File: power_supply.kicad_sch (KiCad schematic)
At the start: 59 parts, among them Q1201 2N7002, Q1202 DMP3037LSS, U1201 TL431PK, U1202 TL431PK, U1203 TL431PK, U1204 MCP1825T-330, U1205 NCV8164ASN120T1G, U1206 MCP1825T-330, U1207 NCV8164ASN250T1G, U1208 NCV8164ASN330T1G

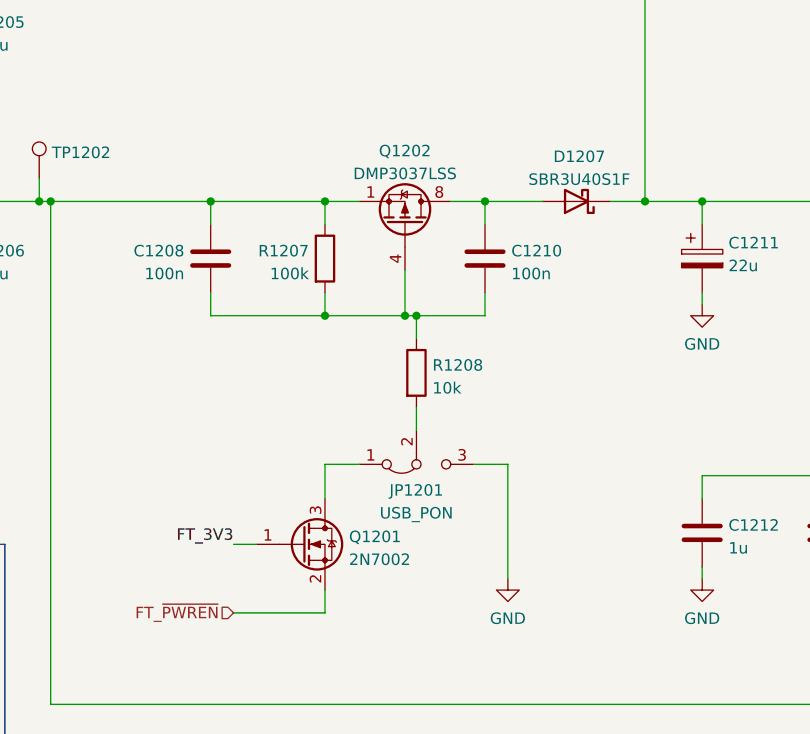
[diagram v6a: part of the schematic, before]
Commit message: Schematic: change mosfets in VBUS switcher
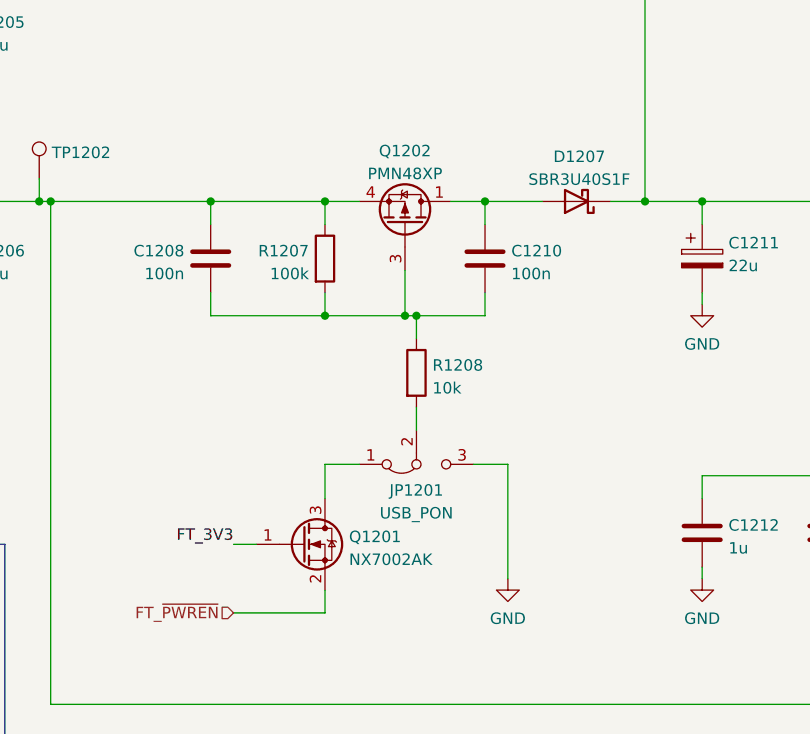
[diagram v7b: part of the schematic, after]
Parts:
- removed Q1202: DMP3037LSS, Package_SO:SOIC-8_3.9x4.9mm_P1.27mm, symbol Transistor_FET:FDS9435A
- added Q1202: PMN48XP, Package_SO:TSOP-6_1.65x3.05mm_P0.95mm, symbol Transistor_FET:PMN48XP
- Q1201: value 2N7002 -> NX7002AK; Mfr PN 2N7002NXAKR -> NX7002AKAR
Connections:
- net OUT_VBUS_CLEAN: now also Q1202.4 (S)
- net at C1210.1, D1207.2 (A): now also Q1202.1 (D), Q1202.2 (D), Q1202.5 (D), Q1202.6 (D)
- net at C1208.2, C1210.2, R1207.2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: now also Q1202.3 (G)
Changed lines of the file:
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@@
       (effects (font (size 1.27 1.27)) (justify left))
     )
-    (property "Value" "2N7002" (id 1) (at 127.127 141.4022 0)
+    (property "Value" "NX7002AK" (id 1) (at 127.127 141.4022 0)
       (effects (font (size 1.27 1.27)) (justify left))
     )
@@
       (effects (font (size 1.27 1.27)) hide)
     )
-    (property "Mfr PN" "2N7002NXAKR" (id 5) (at 121.92 139.7 0)
+    (property "Mfr PN" "NX7002AKAR" (id 5) (at 121.92 139.7 0)
       (effects (font (size 1.27 1.27)) hide)
     )
@@
     (pin "2")
   )
-  (symbol (lib_id "Transistor_FET:FDS9435A") (at 133.35 104.14 270) (mirror x) (unit 1)
+  (symbol (lib_id "Device:R") (at 186.69 123.19 270) (unit 1)
+    (in_bom yes) (on_board yes) (fields_autoplaced)
+    (property "Reference" "R1212" (id 0) (at 186.69 118.4742 90))
+    (property "Value" "10k" (id 1) (at 186.69 121.0111 90))
+    (property "Footprint" "Resistor_SMD:R_0805_2012Metric" (id 2) (at 186.69 121.412 90)
+      (effects (font (size 1.27 1.27)) hide)
+    )
+    (property "Datasheet" "~" (id 3) (at 186.69 123.19 0)
+      (effects (font (size 1.27 1.27)) hide)
+    )
+    (property "Tolerance" "" (id 4) (at 186.69 123.19 0)
+      (effects (font (size 1.27 1.27)) hide)
+    )
+    (pin "1")
+    (pin "2")
+  )
+  (symbol (lib_id "power:GND") (at 129.54 36.83 0) (unit 1)
+    (in_bom yes) (on_board yes) (fields_autoplaced)
+    (property "Reference" "#PWR01214" (id 0) (at 129.54 43.18 0)
+      (effects (font (size 1.27 1.27)) hide)
+    )
+    (property "Value" "GND" (id 1) (at 129.54 41.2734 0))
+    (property "Footprint" "" (id 2) (at 129.54 36.83 0)
+      (effects (font (size 1.27 1.27)) hide)
+    )
+    (property "Datasheet" "" (id 3) (at 129.54 36.83 0)
+      (effects (font (size 1.27 1.27)) hide)
+    )
+    (pin "1")
+  )
+  (symbol (lib_id "Transistor_FET:PMN48XP") (at 133.35 104.14 270) (mirror x) (unit 1)
     (in_bom yes) (on_board yes) (fields_autoplaced)
     (property "Reference" "Q1202" (id 0) (at 133.35 95.9952 90))
-    (property "Value" "DMP3037LSS" (id 1) (at 133.35 98.5321 90))
-    (property "Footprint" "Package_SO:SOIC-8_3.9x4.9mm_P1.27mm" (id 2) (at 131.445 99.06 0)
-      (effects (font (size 1.27 1.27) italic) (justify left) hide)
-    )
-    (property "Datasheet" "https://www.diodes.com/assets/Datasheets/DMP3037LSS.pdf" (id 3) (at 133.35 104.14 90)
+    (property "Value" "PMN48XP" (id 1) (at 133.35 98.5321 90))
+    (property "Footprint" "Package_SO:TSOP-6_1.65x3.05mm_P0.95mm" (id 2) (at 130.81 99.06 0)
       (effects (font (size 1.27 1.27)) (justify left) hide)
     )
-    (property "Mfr" "DIODES" (id 4) (at 133.35 104.14 0)
-      (effects (font (size 1.27 1.27)) hide)
-    )
-    (property "Mfr PN" "DMP3037LSS" (id 5) (at 133.35 104.14 0)
+    (property "Datasheet" "https://assets.nexperia.com/documents/data-sheet/PMN48XP.pdf" (id 3) (at 133.35 104.14 0)
+      (effects (font (size 1.27 1.27)) hide)
+    )
+    (property "Mfr" "Nexperia" (id 4) (at 133.35 104.14 0)
+      (effects (font (size 1.27 1.27)) hide)
+    )
+    (property "Mfr PN" "PMN48XP,125" (id 5) (at 133.35 104.14 0)
       (effects (font (size 1.27 1.27)) hide)
     )
@@
     (pin "5")
     (pin "6")
-    (pin "7")
-    (pin "8")
-  )
-  (symbol (lib_id "Device:R") (at 186.69 123.19 270) (unit 1)
-    (in_bom yes) (on_board yes) (fields_autoplaced)
-    (property "Reference" "R1212" (id 0) (at 186.69 118.4742 90))
-    (property "Value" "10k" (id 1) (at 186.69 121.0111 90))
-    (property "Footprint" "Resistor_SMD:R_0805_2012Metric" (id 2) (at 186.69 121.412 90)
-      (effects (font (size 1.27 1.27)) hide)
-    )
-    (property "Datasheet" "~" (id 3) (at 186.69 123.19 0)
-      (effects (font (size 1.27 1.27)) hide)
-    )
-    (property "Tolerance" "" (id 4) (at 186.69 123.19 0)
-      (effects (font (size 1.27 1.27)) hide)
-    )
-    (pin "1")
-    (pin "2")
-  )
-  (symbol (lib_id "power:GND") (at 129.54 36.83 0) (unit 1)
-    (in_bom yes) (on_board yes) (fields_autoplaced)
-    (property "Reference" "#PWR01214" (id 0) (at 129.54 43.18 0)
-      (effects (font (size 1.27 1.27)) hide)
-    )
-    (property "Value" "GND" (id 1) (at 129.54 41.2734 0))
-    (property "Footprint" "" (id 2) (at 129.54 36.83 0)
-      (effects (font (size 1.27 1.27)) hide)
-    )
-    (property "Datasheet" "" (id 3) (at 129.54 36.83 0)
-      (effects (font (size 1.27 1.27)) hide)
-    )
-    (pin "1")
   )
   (symbol (lib_id "power:GND") (at 208.28 116.84 0) (unit 1)

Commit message: Schematic: add PNs for resistors
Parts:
- R1201, R1203: Mfr (none) -> Bourns; Mfr PN (none) -> CR0805-FX-1001ELF
- R1202, R1204, R1206: Mfr (none) -> Bourns; Mfr PN (none) -> CR0805-FX-2401ELF
- R1205: Mfr (none) -> Bourns; Mfr PN (none) -> CR0805-FX-2200ELF
- R1207: Mfr (none) -> Bourns; Mfr PN (none) -> CR0805-FX-1003ELF
- R1208, R1209, R1210, R1211, R1212: Mfr (none) -> Bourns; Mfr PN (none) -> CR0805-FX-1002ELF
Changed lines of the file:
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@@
+      (effects (font (size 1.27 1.27)) hide)
+    )
+    (property "Mfr" "Bourns" (id 5) (at 186.69 95.25 0)
+      (effects (font (size 1.27 1.27)) hide)
+    )
+    (property "Mfr PN" "CR0805-FX-1002ELF" (id 6) (at 186.69 95.25 0)
       (effects (font (size 1.27 1.27)) hide)
     )
@@
     )
     (property "Tolerance" "" (id 4) (at 25.4 170.18 0)
+      (effects (font (size 1.27 1.27)) hide)
+    )
+    (property "Mfr" "Bourns" (id 5) (at 25.4 170.18 0)
+      (effects (font (size 1.27 1.27)) hide)
+    )
+    (property "Mfr PN" "CR0805-FX-2401ELF" (id 6) (at 25.4 170.18 0)
       (effects (font (size 1.27 1.27)) hide)
     )
@@
       (effects (font (size 1.27 1.27)) hide)
     )
+    (property "Mfr" "Bourns" (id 5) (at 186.69 52.07 0)
+      (effects (font (size 1.27 1.27)) hide)
+    )
+    (property "Mfr PN" "CR0805-FX-1002ELF" (id 6) (at 186.69 52.07 0)
+      (effects (font (size 1.27 1.27)) hide)
+    )
     (pin "1")
     (pin "2")
@@
       (effects (font (size 1.27 1.27)) hide)
     )
+    (property "Mfr" "Bourns" (id 5) (at 71.12 170.18 0)
+      (effects (font (size 1.27 1.27)) hide)
+    )
+    (property "Mfr PN" "CR0805-FX-2401ELF" (id 6) (at 71.12 170.18 0)
+      (effects (font (size 1.27 1.27)) hide)
+    )
     (pin "1")
     (pin "2")
@@
     )
     (property "Tolerance" "" (id 4) (at 134.62 120.65 0)
+      (effects (font (size 1.27 1.27)) hide)
+    )
+    (property "Mfr" "Bourns" (id 5) (at 134.62 120.65 0)
+      (effects (font (size 1.27 1.27)) hide)
+    )
+    (property "Mfr PN" "CR0805-FX-1002ELF" (id 6) (at 134.62 120.65 0)
       (effects (font (size 1.27 1.27)) hide)
     )
@@
       (effects (font (size 1.27 1.27)) hide)
     )
+    (property "Mfr" "Bourns" (id 5) (at 186.69 67.31 0)
+      (effects (font (size 1.27 1.27)) hide)
+    )
+    (property "Mfr PN" "CR0805-FX-1002ELF" (id 6) (at 186.69 67.31 0)
+      (effects (font (size 1.27 1.27)) hide)
+    )
     (pin "1")
     (pin "2")
@@
     )
     (property "Tolerance" "" (id 4) (at 48.26 170.18 0)
+      (effects (font (size 1.27 1.27)) hide)
+    )
+    (property "Mfr" "Bourns" (id 5) (at 48.26 170.18 0)
+      (effects (font (size 1.27 1.27)) hide)
+    )
+    (property "Mfr PN" "CR0805-FX-2401ELF" (id 6) (at 48.26 170.18 0)
       (effects (font (size 1.27 1.27)) hide)
     )
@@
       (effects (font (size 1.27 1.27)) hide)
     )
+    (property "Mfr" "Bourns" (id 5) (at 71.12 160.02 0)
+      (effects (font (size 1.27 1.27)) hide)
+    )
+    (property "Mfr PN" "CR0805-FX-2200ELF" (id 6) (at 71.12 160.02 0)
+      (effects (font (size 1.27 1.27)) hide)
+    )
     (pin "1")
     (pin "2")
@@
       (effects (font (size 1.27 1.27)) hide)
     )
+    (property "Mfr" "Bourns" (id 5) (at 124.46 107.95 0)
+      (effects (font (size 1.27 1.27)) hide)
+    )
+    (property "Mfr PN" "CR0805-FX-1003ELF" (id 6) (at 124.46 107.95 0)
+      (effects (font (size 1.27 1.27)) hide)
+    )
     (pin "1")
     (pin "2")
@@
       (effects (font (size 1.27 1.27)) hide)
     )
+    (property "Mfr" "Bourns" (id 5) (at 48.26 160.02 0)
+      (effects (font (size 1.27 1.27)) hide)
+    )
+    (property "Mfr PN" "CR0805-FX-1001ELF" (id 6) (at 48.26 160.02 0)
+      (effects (font (size 1.27 1.27)) hide)
+    )
     (pin "1")
     (pin "2")
@@
     )
     (property "Tolerance" "" (id 4) (at 25.4 160.02 0)
+      (effects (font (size 1.27 1.27)) hide)
+    )
+    (property "Mfr" "Bourns" (id 5) (at 25.4 160.02 0)
+      (effects (font (size 1.27 1.27)) hide)
+    )
+    (property "Mfr PN" "CR0805-FX-1001ELF" (id 6) (at 25.4 160.02 0)
       (effects (font (size 1.27 1.27)) hide)
     )
@@
       (effects (font (size 1.27 1.27)) hide)
     )
+    (property "Mfr" "Bourns" (id 5) (at 186.69 123.19 0)
+      (effects (font (size 1.27 1.27)) hide)
+    )
+    (property "Mfr PN" "CR0805-FX-1002ELF" (id 6) (at 186.69 123.19 0)
+      (effects (font (size 1.27 1.27)) hide)
+    )
